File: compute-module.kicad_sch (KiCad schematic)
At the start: 96 parts, among them J1 DF40HC(3.0)-100DS-0.4v, J2 DF40HC(3.0)-100DS-0.4v, M1 compute-module-4-1.5mm

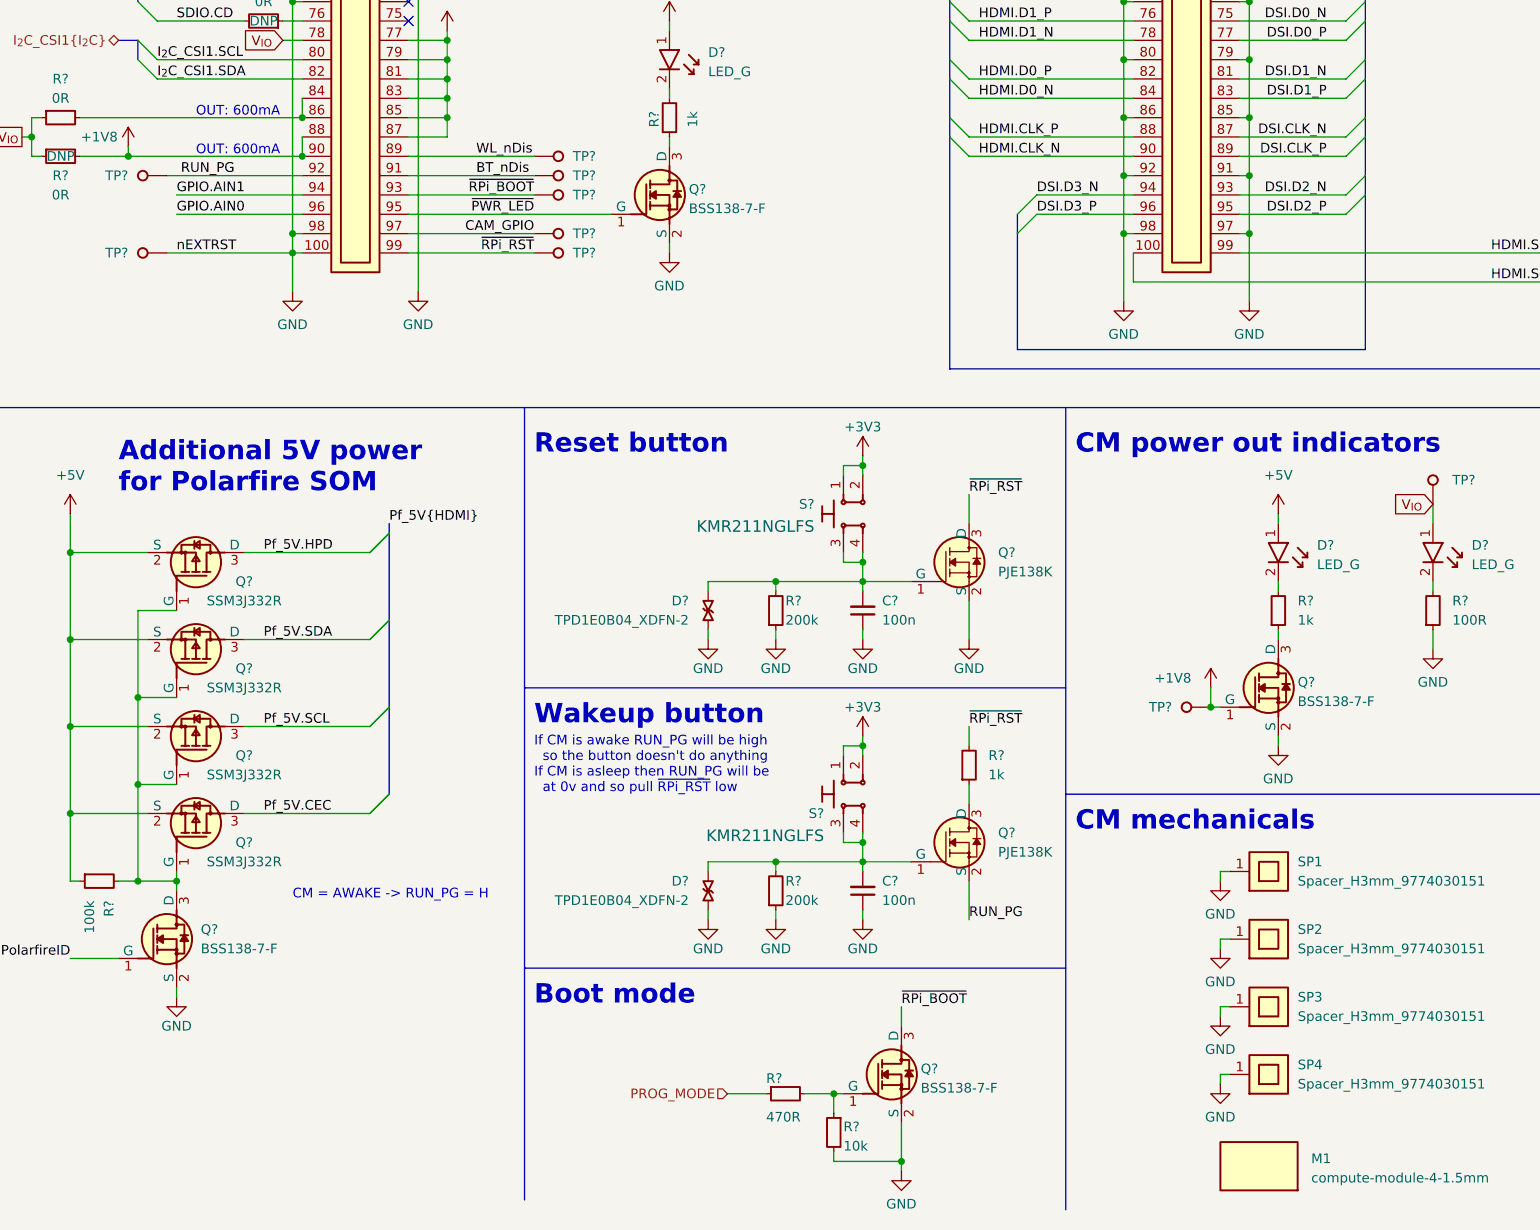
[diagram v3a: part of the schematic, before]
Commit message: [#54617] Change all NMOS to be single MPN
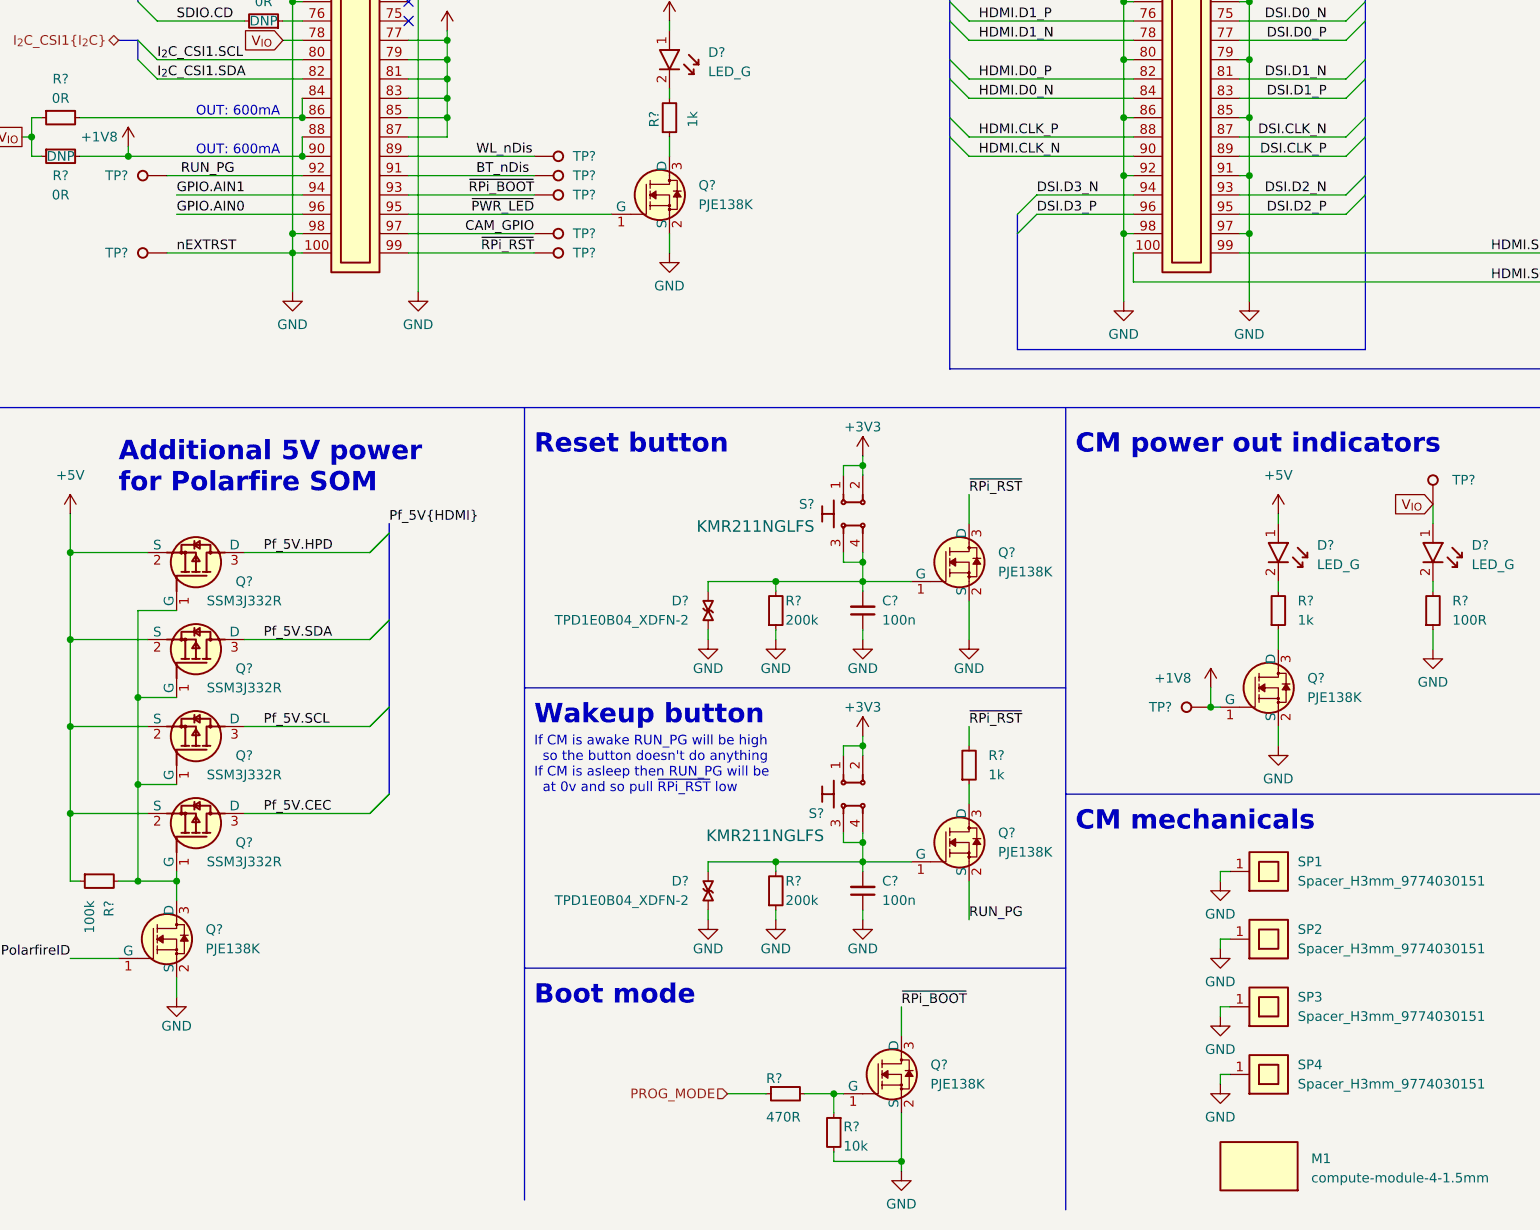
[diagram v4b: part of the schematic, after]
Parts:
- Q? (x4): value BSS138-7-F -> PJE138K; footprint antmicro-footprints:SOT-23-3 -> antmicro-footprints:SOT-523; symbol antmicroTransistorsFETsMOSFETsSingle:BSS138-7-F -> antmicroTransistorsFETsMOSFETsSingle:PJE138K; MPN BSS138-7-F -> PJE138K_R1_00001; Manufacturer Diodes Incorporated -> PANJIT
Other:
- note removed: "CM = AWAKE -> RUN_PG = H"

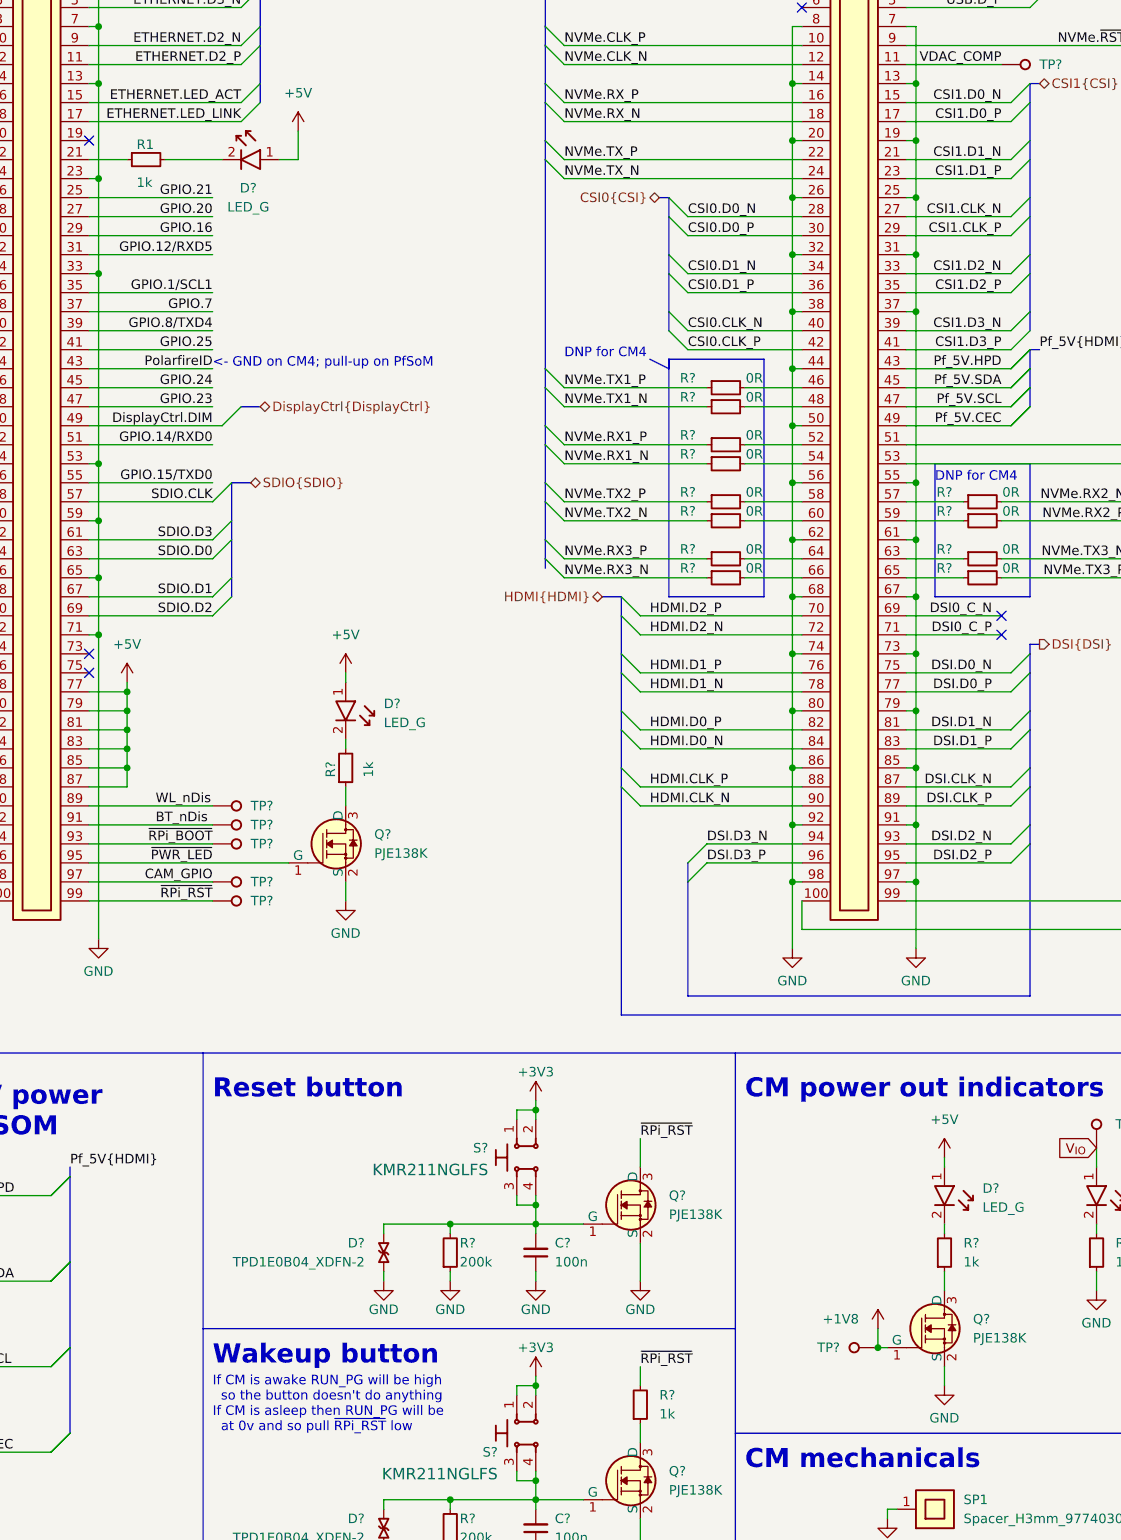
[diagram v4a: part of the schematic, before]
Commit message: [#54617] Reduce resistors diversity (switch size to 0402)
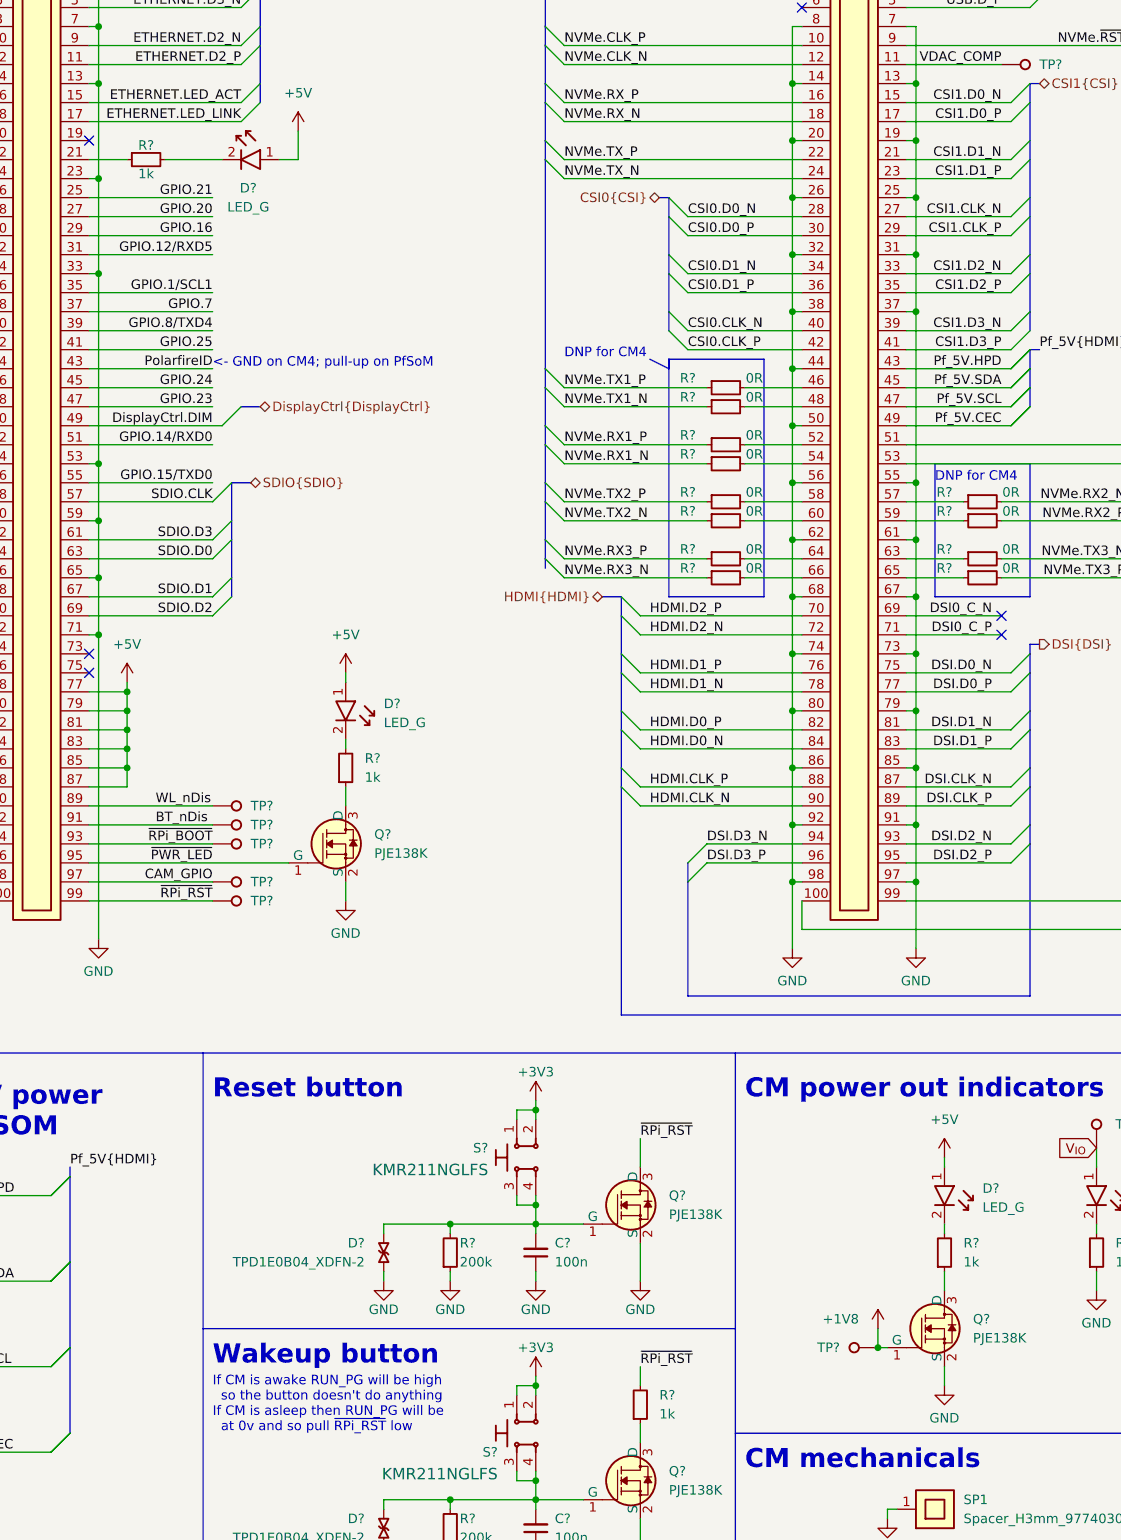
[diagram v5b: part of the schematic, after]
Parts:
- removed R1, R? (x3): R_1k_0603, antmicro-footprints:R_0603_1608Metric, symbol antmicroResistors0603:R_1k_0603
- added R? (x4): R_1k_0402, antmicro-footprints:R_0402_1005Metric, symbol antmicroResistors0402:R_1k_0402
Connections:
- net ~{RPi_RST}: now also R?.2
- net at J1.21: now also R?.1
- net at D?.2: now also R?.2 (x3)
- net at Q?.3 (D): now also R?.1 (x3)

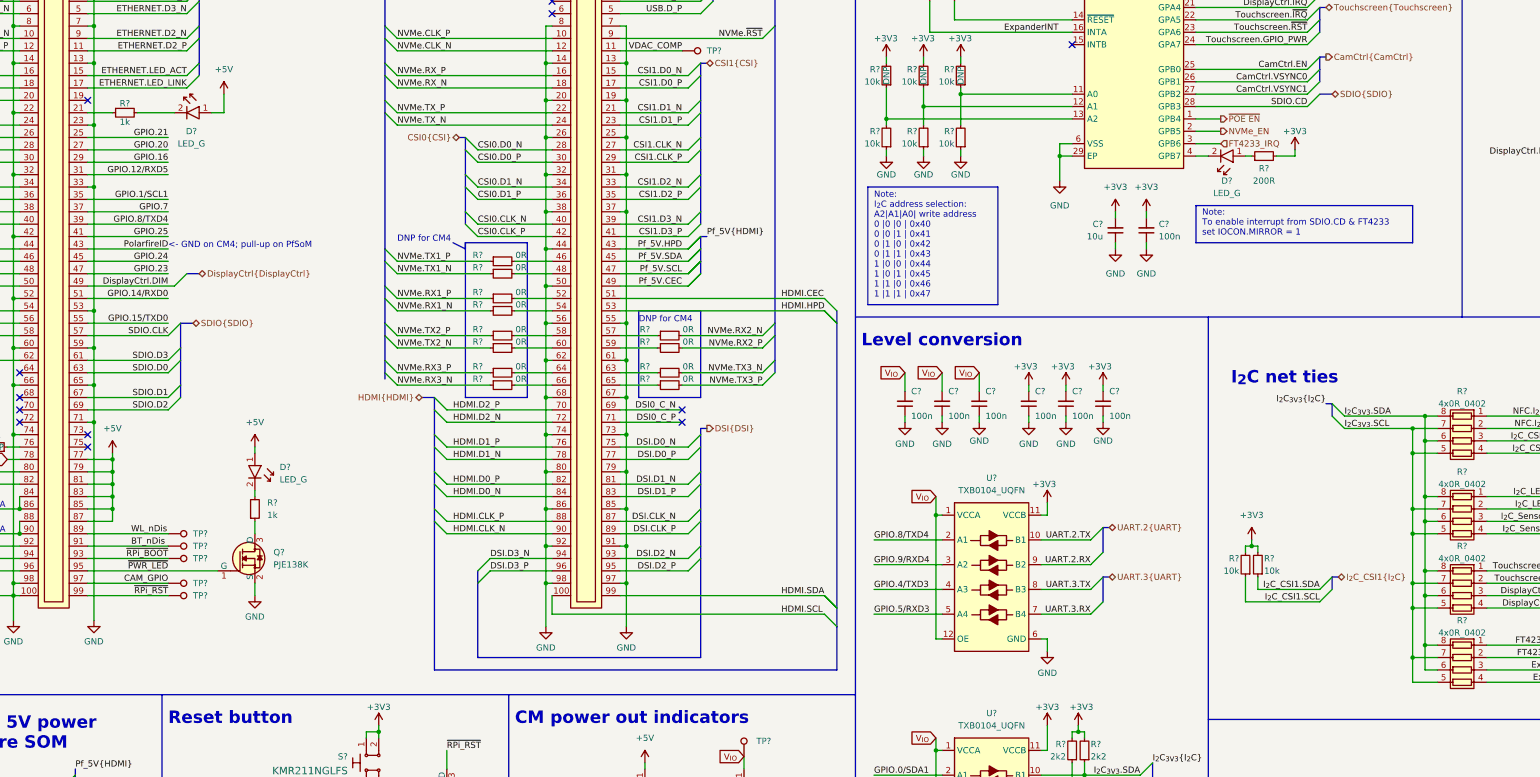
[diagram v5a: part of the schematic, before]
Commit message: [#54617] Connect VSYNC0/1 & WKUP_REQ through 0R-DNP to CM
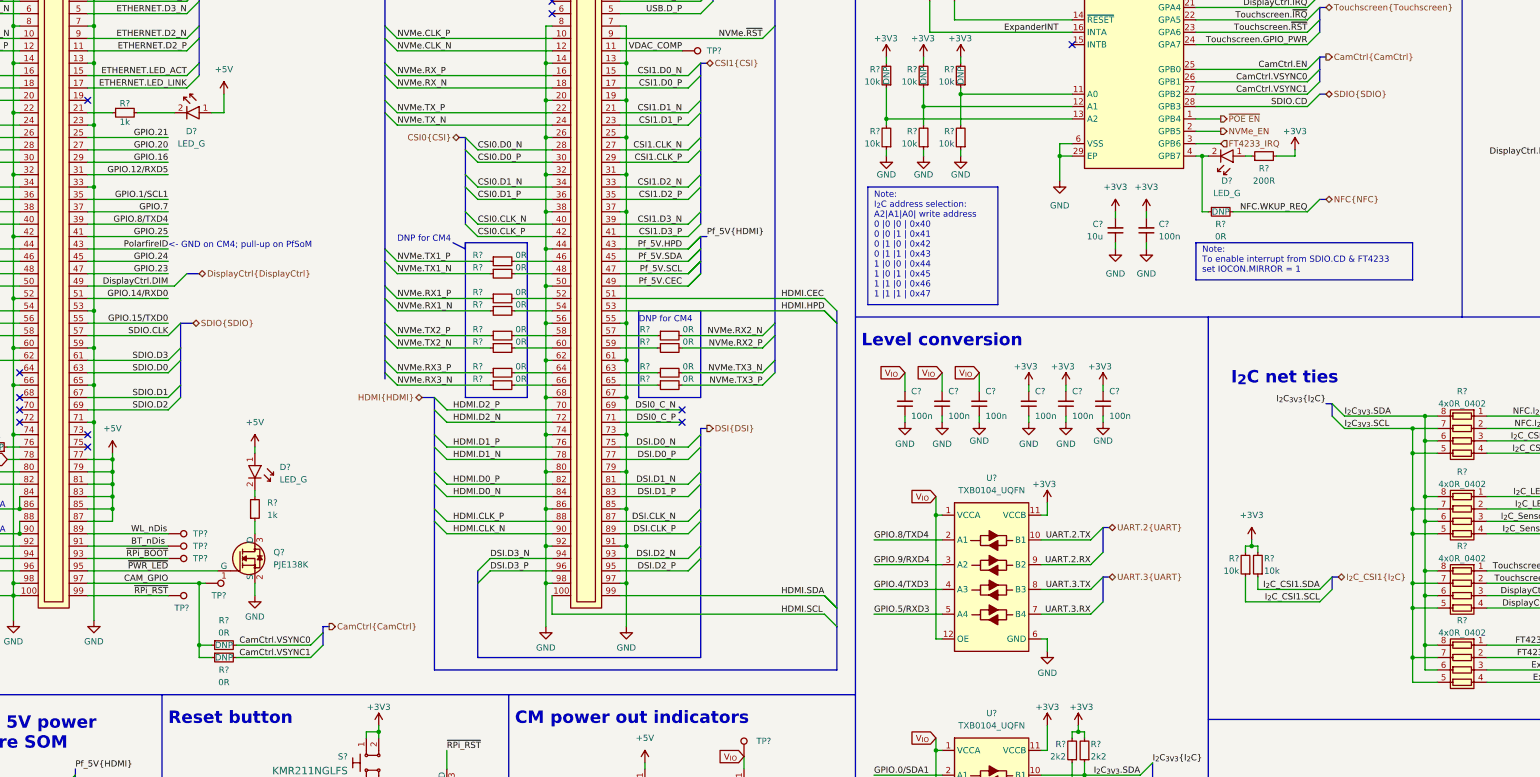
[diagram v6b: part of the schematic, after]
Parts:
- added R? (x3): R_0R_0402, antmicro-footprints:R_0402_1005Metric, symbol antmicroResistors0402:R_0R_0402
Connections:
- net CAM_GPIO: now also R?.1, R?.1
- net CamCtrl.VSYNC0: now also R?.2
- net CamCtrl.VSYNC1: now also R?.2
- net at D?.2, U?.4 (GPB7): now also R?.1
- new net NFC.WKUP_REQ: R?.2
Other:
- moved on the sheet: TP?
